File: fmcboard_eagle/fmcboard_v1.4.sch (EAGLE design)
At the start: 160 parts, among them IC1 OPA699ID, IC10 LTC6229IMS8E#TRPBF, IC11 7805TV, IC12 SN74AUC2G66DCTR, IC13 SN74AUC2G66DCTR, IC14 SN74AUC2G66DCTR, IC15 SN74AUC2G66DCTR, IC16 DAC7578SPWR, IC2 DAC7578SPWR, IC3 LTC6229IMS8E#TRPBF, IC4 LTC6229IMS8E#TRPBF, IC5 LM358, IC6 OPA699ID, IC7 OPA699ID, IC8 LTC6229IMS8E#TRPBF, IC9 LTC6229IMS8E#TRPBF, J1 8pin, J10 8pin, J12 4p-2.54, J2 ASP-134604-01, J3 4p-2.54, J4 4p-2.54, J5 8pin, J6 4p-2.54, J7 4p-2.54, J8 4p-2.54, J9 8pin, U1 TXS0108EPWR, U2 STMICROELECTRONICS_L7905ACVST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

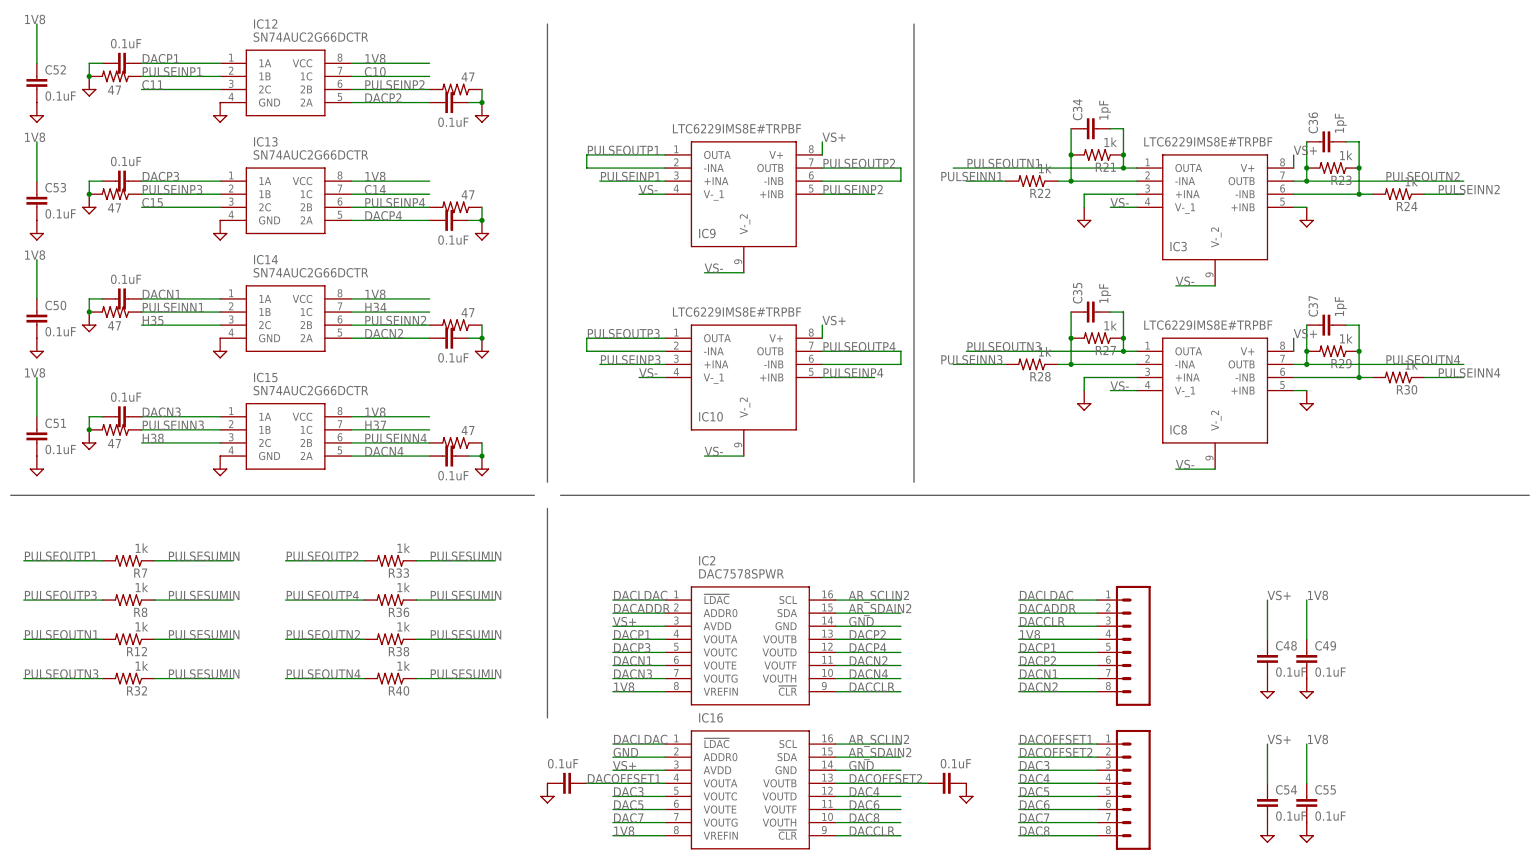
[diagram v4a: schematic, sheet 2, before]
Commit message: 100 Ohm neg pulse and neg sum feedback resistors 4.7k->1k transimpedance resistor
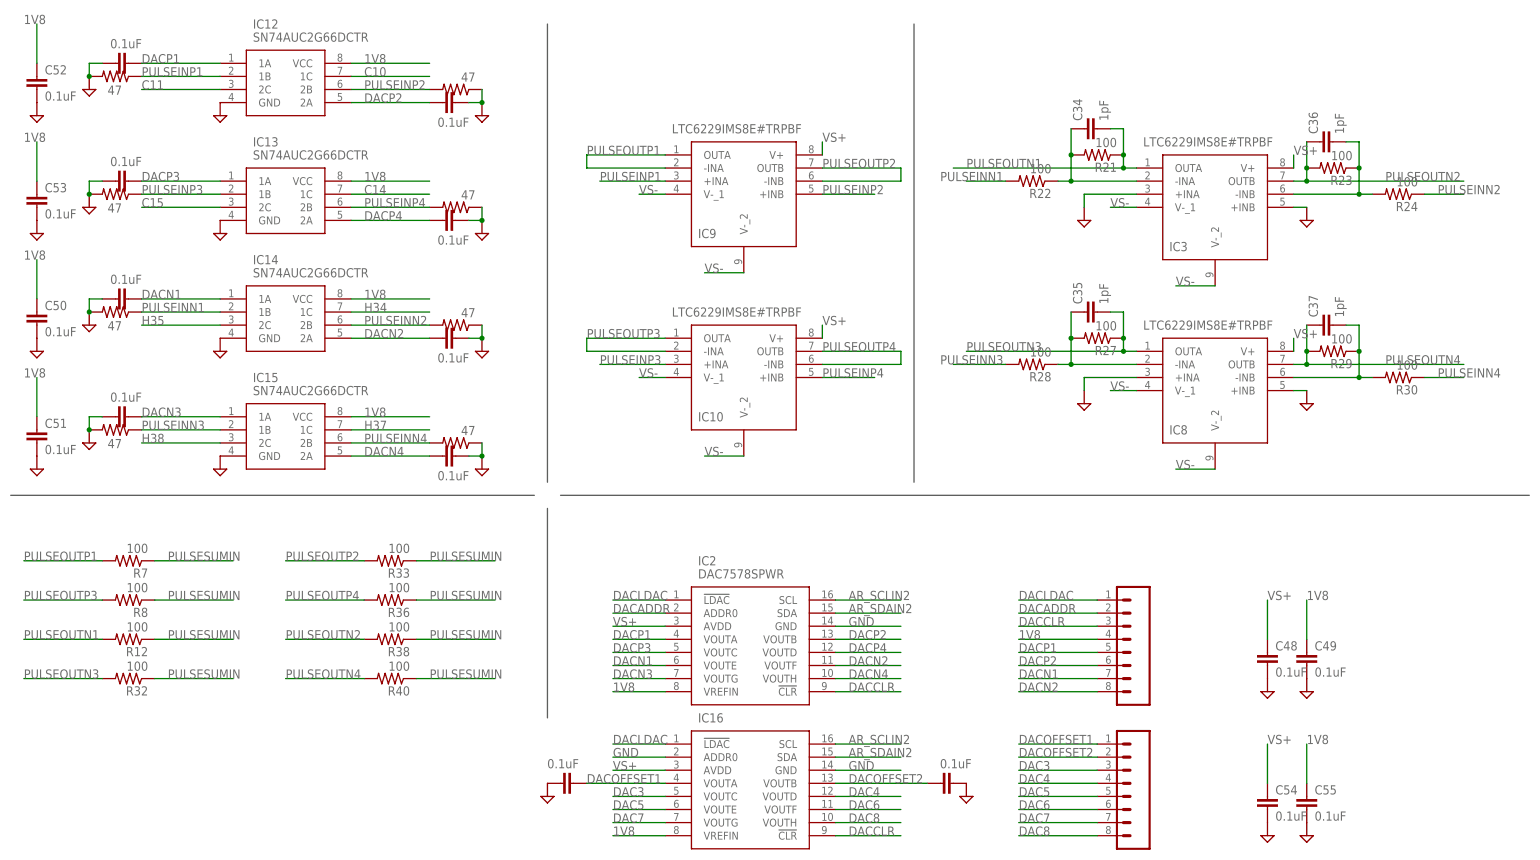
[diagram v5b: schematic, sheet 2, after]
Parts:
- R1, R12, R21, R22, R23, R24, R27, R28, R29, R30, R32, R33, R36, R38, R40, R7, R8: value 1k -> 100
- R11: value 4.7k -> 1k
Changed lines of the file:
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@@
 <part name="IC5" library="SparkFun-AnalogIC" deviceset="LM358" device=""/>
 <part name="SUPPLY20" library="supply2" library_urn="urn:adsk.eagle:library:372" deviceset="GND" device=""/>
-<part name="R21" library="rcl" library_urn="urn:adsk.eagle:library:334" deviceset="R-US_" device="R0805" package3d_urn="urn:adsk.eagle:package:23553/2" value="1k"/>
-<part name="R22" library="rcl" library_urn="urn:adsk.eagle:library:334" deviceset="R-US_" device="R0805" package3d_urn="urn:adsk.eagle:package:23553/2" value="1k"/>
+<part name="R21" library="rcl" library_urn="urn:adsk.eagle:library:334" deviceset="R-US_" device="R0805" package3d_urn="urn:adsk.eagle:package:23553/2" value="100"/>
+<part name="R22" library="rcl" library_urn="urn:adsk.eagle:library:334" deviceset="R-US_" device="R0805" package3d_urn="urn:adsk.eagle:package:23553/2" value="100"/>
 <part name="IC3" library="LTC6229IMS8E#TRPBF" deviceset="LTC6229IMS8E#TRPBF" device=""/>
-<part name="R23" library="rcl" library_urn="urn:adsk.eagle:library:334" deviceset="R-US_" device="R0805" package3d_urn="urn:adsk.eagle:package:23553/2" value="1k"/>
-<part name="R24" library="rcl" library_urn="urn:adsk.eagle:library:334" deviceset="R-US_" device="R0805" package3d_urn="urn:adsk.eagle:package:23553/2" value="1k"/>
+<part name="R23" library="rcl" library_urn="urn:adsk.eagle:library:334" deviceset="R-US_" device="R0805" package3d_urn="urn:adsk.eagle:package:23553/2" value="100"/>
+<part name="R24" library="rcl" library_urn="urn:adsk.eagle:library:334" deviceset="R-US_" device="R0805" package3d_urn="urn:adsk.eagle:package:23553/2" value="100"/>
 <part name="SUPPLY32" library="supply2" library_urn="urn:adsk.eagle:library:372" deviceset="GND" device=""/>
 <part name="SUPPLY21" library="supply2" library_urn="urn:adsk.eagle:library:372" deviceset="GND" device=""/>
-<part name="R11" library="rcl" library_urn="urn:adsk.eagle:library:334" deviceset="R-US_" device="R0805" package3d_urn="urn:adsk.eagle:package:23553/2" value="4.7k"/>
+<part name="R11" library="rcl" library_urn="urn:adsk.eagle:library:334" deviceset="R-US_" device="R0805" package3d_urn="urn:adsk.eagle:package:23553/2" value="1k"/>
 <part name="IC4" library="LTC6229IMS8E#TRPBF" deviceset="LTC6229IMS8E#TRPBF" device=""/>
 <part name="C4" library="SparkFun-Passives" deviceset="CAP" device="0805" value="0.1uF"/>
@@
 <part name="R26" library="rcl" library_urn="urn:adsk.eagle:library:334" deviceset="R-US_" device="R0805" package3d_urn="urn:adsk.eagle:package:23553/2" value="200"/>
 <part name="SUPPLY33" library="supply2" library_urn="urn:adsk.eagle:library:372" deviceset="GND" device=""/>
-<part name="R27" library="rcl" library_urn="urn:adsk.eagle:library:334" deviceset="R-US_" device="R0805" package3d_urn="urn:adsk.eagle:package:23553/2" value="1k"/>
-<part name="R28" library="rcl" library_urn="urn:adsk.eagle:library:334" deviceset="R-US_" device="R0805" package3d_urn="urn:adsk.eagle:package:23553/2" value="1k"/>
+<part name="R27" library="rcl" library_urn="urn:adsk.eagle:library:334" deviceset="R-US_" device="R0805" package3d_urn="urn:adsk.eagle:package:23553/2" value="100"/>
+<part name="R28" library="rcl" library_urn="urn:adsk.eagle:library:334" deviceset="R-US_" device="R0805" package3d_urn="urn:adsk.eagle:package:23553/2" value="100"/>
 <part name="IC8" library="LTC6229IMS8E#TRPBF" deviceset="LTC6229IMS8E#TRPBF" device=""/>
-<part name="R29" library="rcl" library_urn="urn:adsk.eagle:library:334" deviceset="R-US_" device="R0805" package3d_urn="urn:adsk.eagle:package:23553/2" value="1k"/>
-<part name="R30" library="rcl" library_urn="urn:adsk.eagle:library:334" deviceset="R-US_" device="R0805" package3d_urn="urn:adsk.eagle:package:23553/2" value="1k"/>
+<part name="R29" library="rcl" library_urn="urn:adsk.eagle:library:334" deviceset="R-US_" device="R0805" package3d_urn="urn:adsk.eagle:package:23553/2" value="100"/>
+<part name="R30" library="rcl" library_urn="urn:adsk.eagle:library:334" deviceset="R-US_" device="R0805" package3d_urn="urn:adsk.eagle:package:23553/2" value="100"/>
 <part name="SUPPLY35" library="supply2" library_urn="urn:adsk.eagle:library:372" deviceset="GND" device=""/>
 <part name="IC9" library="LTC6229IMS8E#TRPBF" deviceset="LTC6229IMS8E#TRPBF" device=""/>
@@
 <part name="SUPPLY67" library="supply2" library_urn="urn:adsk.eagle:library:372" deviceset="GND" device=""/>
 <part name="SUPPLY68" library="supply2" library_urn="urn:adsk.eagle:library:372" deviceset="GND" device=""/>
-<part name="R1" library="rcl" library_urn="urn:adsk.eagle:library:334" deviceset="R-US_" device="R0805" package3d_urn="urn:adsk.eagle:package:23553/2" value="1k"/>
-<part name="R7" library="rcl" library_urn="urn:adsk.eagle:library:334" deviceset="R-US_" device="R0805" package3d_urn="urn:adsk.eagle:package:23553/2" value="1k"/>
-<part name="R8" library="rcl" library_urn="urn:adsk.eagle:library:334" deviceset="R-US_" device="R0805" package3d_urn="urn:adsk.eagle:package:23553/2" value="1k"/>
-<part name="R12" library="rcl" library_urn="urn:adsk.eagle:library:334" deviceset="R-US_" device="R0805" package3d_urn="urn:adsk.eagle:package:23553/2" value="1k"/>
-<part name="R32" library="rcl" library_urn="urn:adsk.eagle:library:334" deviceset="R-US_" device="R0805" package3d_urn="urn:adsk.eagle:package:23553/2" value="1k"/>
-<part name="R33" library="rcl" library_urn="urn:adsk.eagle:library:334" deviceset="R-US_" device="R0805" package3d_urn="urn:adsk.eagle:package:23553/2" value="1k"/>
-<part name="R36" library="rcl" library_urn="urn:adsk.eagle:library:334" deviceset="R-US_" device="R0805" package3d_urn="urn:adsk.eagle:package:23553/2" value="1k"/>
-<part name="R38" library="rcl" library_urn="urn:adsk.eagle:library:334" deviceset="R-US_" device="R0805" package3d_urn="urn:adsk.eagle:package:23553/2" value="1k"/>
-<part name="R40" library="rcl" library_urn="urn:adsk.eagle:library:334" deviceset="R-US_" device="R0805" package3d_urn="urn:adsk.eagle:package:23553/2" value="1k"/>
+<part name="R1" library="rcl" library_urn="urn:adsk.eagle:library:334" deviceset="R-US_" device="R0805" package3d_urn="urn:adsk.eagle:package:23553/2" value="100"/>
+<part name="R7" library="rcl" library_urn="urn:adsk.eagle:library:334" deviceset="R-US_" device="R0805" package3d_urn="urn:adsk.eagle:package:23553/2" value="100"/>
+<part name="R8" library="rcl" library_urn="urn:adsk.eagle:library:334" deviceset="R-US_" device="R0805" package3d_urn="urn:adsk.eagle:package:23553/2" value="100"/>
+<part name="R12" library="rcl" library_urn="urn:adsk.eagle:library:334" deviceset="R-US_" device="R0805" package3d_urn="urn:adsk.eagle:package:23553/2" value="100"/>
+<part name="R32" library="rcl" library_urn="urn:adsk.eagle:library:334" deviceset="R-US_" device="R0805" package3d_urn="urn:adsk.eagle:package:23553/2" value="100"/>
+<part name="R33" library="rcl" library_urn="urn:adsk.eagle:library:334" deviceset="R-US_" device="R0805" package3d_urn="urn:adsk.eagle:package:23553/2" value="100"/>
+<part name="R36" library="rcl" library_urn="urn:adsk.eagle:library:334" deviceset="R-US_" device="R0805" package3d_urn="urn:adsk.eagle:package:23553/2" value="100"/>
+<part name="R38" library="rcl" library_urn="urn:adsk.eagle:library:334" deviceset="R-US_" device="R0805" package3d_urn="urn:adsk.eagle:package:23553/2" value="100"/>
+<part name="R40" library="rcl" library_urn="urn:adsk.eagle:library:334" deviceset="R-US_" device="R0805" package3d_urn="urn:adsk.eagle:package:23553/2" value="100"/>
 <part name="SUPPLY25" library="supply2" library_urn="urn:adsk.eagle:library:372" deviceset="GND" device=""/>
 <part name="R2" library="rcl" library_urn="urn:adsk.eagle:library:334" deviceset="R-US_" device="R0805" package3d_urn="urn:adsk.eagle:package:23553/2" value="47"/>

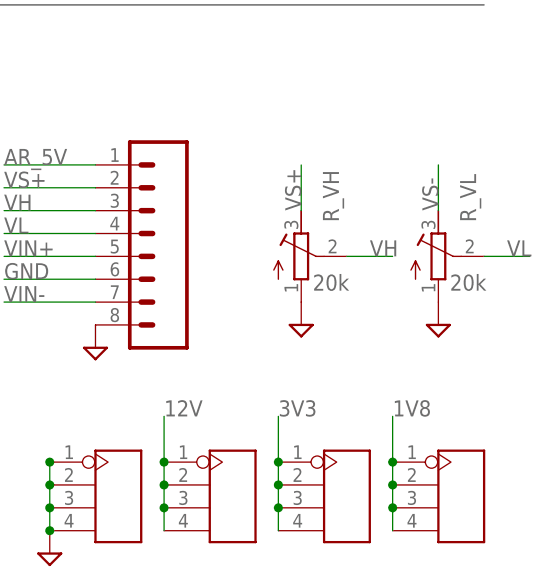
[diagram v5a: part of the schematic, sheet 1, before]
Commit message: 20k -> 5k pots
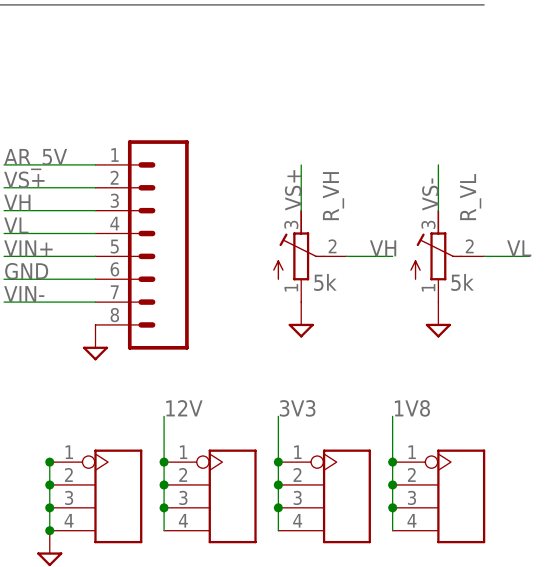
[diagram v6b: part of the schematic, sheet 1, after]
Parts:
- R_O1, R_O2, R_VH, R_VL: value 20k -> 5k
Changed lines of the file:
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@@
 <part name="SUPPLY17" library="supply2" library_urn="urn:adsk.eagle:library:372" deviceset="GND" device=""/>
 <part name="SUPPLY18" library="supply2" library_urn="urn:adsk.eagle:library:372" deviceset="GND" device=""/>
-<part name="R_VH" library="resistor" library_urn="urn:adsk.eagle:library:348" deviceset="R-TRIMM" device="3296W" package3d_urn="urn:adsk.eagle:package:26033/1" value="20k"/>
-<part name="R_VL" library="resistor" library_urn="urn:adsk.eagle:library:348" deviceset="R-TRIMM" device="3296W" package3d_urn="urn:adsk.eagle:package:26033/1" value="20k"/>
+<part name="R_VH" library="resistor" library_urn="urn:adsk.eagle:library:348" deviceset="R-TRIMM" device="3296W" package3d_urn="urn:adsk.eagle:package:26033/1" value="5k"/>
+<part name="R_VL" library="resistor" library_urn="urn:adsk.eagle:library:348" deviceset="R-TRIMM" device="3296W" package3d_urn="urn:adsk.eagle:package:26033/1" value="5k"/>
 <part name="SUPPLY22" library="supply2" library_urn="urn:adsk.eagle:library:372" deviceset="GND" device=""/>
 <part name="SUPPLY23" library="supply2" library_urn="urn:adsk.eagle:library:372" deviceset="GND" device=""/>
@@
 <part name="R13" library="rcl" library_urn="urn:adsk.eagle:library:334" deviceset="R-US_" device="R0805" package3d_urn="urn:adsk.eagle:package:23553/2" value="1k"/>
 <part name="R14" library="rcl" library_urn="urn:adsk.eagle:library:334" deviceset="R-US_" device="R0805" package3d_urn="urn:adsk.eagle:package:23553/2" value="4.7k"/>
-<part name="R_O1" library="resistor" library_urn="urn:adsk.eagle:library:348" deviceset="R-TRIMM" device="3296W" package3d_urn="urn:adsk.eagle:package:26033/1" value="20k"/>
+<part name="R_O1" library="resistor" library_urn="urn:adsk.eagle:library:348" deviceset="R-TRIMM" device="3296W" package3d_urn="urn:adsk.eagle:package:26033/1" value="5k"/>
 <part name="R3" library="rcl" library_urn="urn:adsk.eagle:library:334" deviceset="R-US_" device="R0805" package3d_urn="urn:adsk.eagle:package:23553/2" value="100k"/>
 <part name="IO_G2" library="con-coax" library_urn="urn:adsk.eagle:library:133" deviceset="BU-SMB-V" device="" package3d_urn="urn:adsk.eagle:package:6209/1"/>
@@
 <part name="C4" library="SparkFun-Passives" deviceset="CAP" device="0805" value="0.1uF"/>
 <part name="SUPPLY6" library="supply2" library_urn="urn:adsk.eagle:library:372" deviceset="GND" device=""/>
-<part name="R_O2" library="resistor" library_urn="urn:adsk.eagle:library:348" deviceset="R-TRIMM" device="3296W" package3d_urn="urn:adsk.eagle:package:26033/1" value="20k"/>
+<part name="R_O2" library="resistor" library_urn="urn:adsk.eagle:library:348" deviceset="R-TRIMM" device="3296W" package3d_urn="urn:adsk.eagle:package:26033/1" value="5k"/>
 <part name="R17" library="rcl" library_urn="urn:adsk.eagle:library:334" deviceset="R-US_" device="R0805" package3d_urn="urn:adsk.eagle:package:23553/2" value="100k"/>
 <part name="IC6" library="OPA699ID" deviceset="OPA699ID" device=""/>
